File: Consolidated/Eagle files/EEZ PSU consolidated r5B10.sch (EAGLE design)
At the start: 542 parts, among them IC1 LTC3864EMSE#PBF, IC10 REF5025AIDG4, IC11 DAC8552IDGKTG4, IC12 ADG465SOT-23, IC13 TS5A9411DCKT, IC14 ADS1120IPWR, IC15 LP339D, IC16 LM25575MH/NOPB, IC17 TPD4E002DRLR, IC18 TPD2E001DZDR, IC19 ADUM3160BRWZ, IC2 MC79L05, IC20 TLC5925IDBQR, IC21 Si8641EC-B-IS1, IC22 SI8651EC-B-IS1, IC23 SI8651EC-B-IS1, IC24 LD1117ADT33TR, IC25 Si8641EC-B-IS1, IC26 PCA21125T/Q900/1,1, IC27 AT25256B-SSHL-B, IC28 W5500, IC29 BC857BS, IC3 MC78L05, IC30 TLC555, IC31 SN74LVC2G08DCTR, IC32 TPS3705-33D, IC33 SN74LV1T34DBVR, IC34 SN74LVC2G02DCTR, IC4 LM5574MTX/NOPB, IC5 LP2951SO8, IC6 TL072D, IC7 TL072D, IC8 OP27GSZ, IC9 MCP23S08-E/SO, J1 BS-244DSM-R, J2 BS-244DSM-G, J3 BS-244DSM-B, J4 BS-244DSM-R, J5 BS-244DSM-B, Q1 IRFR5305, Q10 MMBT5401, Q11 MMBT5401, Q12 MMBT5551, Q13 MMBT5551, Q14 BSS84P, Q15 2N7002, Q16 MMBT5551, Q17 MMBT5401, Q18 MMBT5551, Q19 MMBT5551, Q2 MMBT5401, Q20 BTA26-600, Q21 BTA26-600, Q22 IRLL014N, Q23 IRLML2246TRPBF, Q24 IRLML2246TRPBF, Q25 IRLML2246TRPBF, Q26 IRLML2246TRPBF, Q27 2N7002, Q28 IRLML2246TRPBF, Q29 2N7002, Q3 2N7002, Q30 2N7002, Q4 IRFP250N, Q5 BC857C, Q6 BC846C, Q7 BCP56-16.115, Q8 IRFR5410, Q9 BCP56-16.115, SW1 A101SYCQ04, SW2 1301.9316, X1 39303035, X10 826629-5, X11 2411-01, X12 MC000006, X13 TSW-113-07-F-D, X14 MC000005, X15 TSW-113-07-F-D, X16 09185067324, X17 22-23-2021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

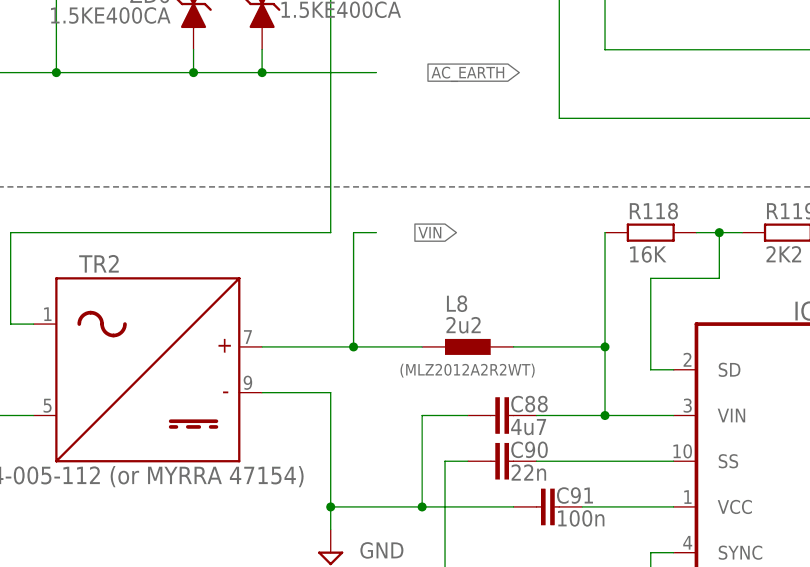
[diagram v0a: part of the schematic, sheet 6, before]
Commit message: r5B10 BOM, top silkscreen minor correction
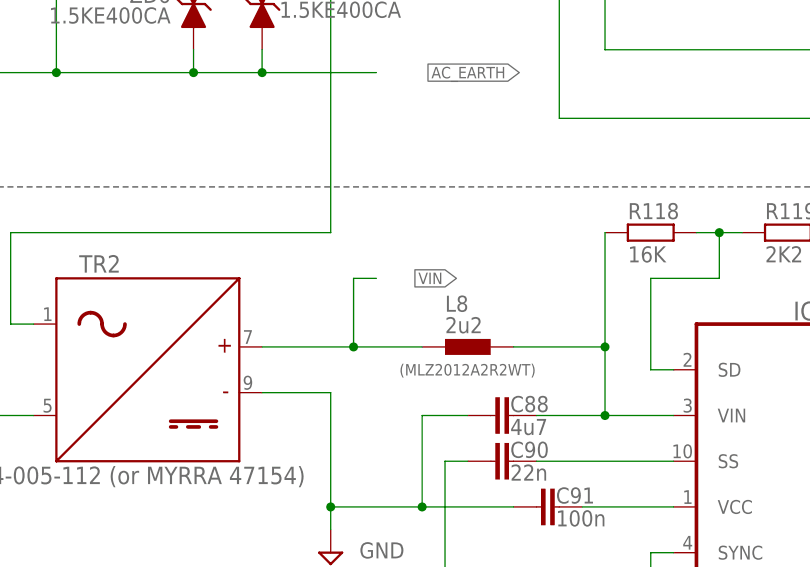
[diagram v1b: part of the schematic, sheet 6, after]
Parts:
- renumbered R136A1 to R140A
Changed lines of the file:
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@@
 <part name="R136A" library="rcl" deviceset="R-EU_" device="R0805" value="1R"/>
 <part name="C109A" library="rcl" deviceset="C-EU" device="C0805" value="1u"/>
-<part name="R136A1" library="rcl" deviceset="R-EU_" device="R0805" value="1R"/>
+<part name="R140A" library="rcl" deviceset="R-EU_" device="R0805" value="1R"/>
 <part name="C111" library="Panasonic-EEEFK_EEEFP" deviceset="EEE-" device="-CASE-E" technology="FK1J220P" value="EEEFK1J220P"/>
 <part name="C106" library="Panasonic-EEEFK_EEEFP" deviceset="EEE-" device="-CASE-E" technology="FK1J220P" value="EEEFK1J220P"/>
@@
 <pinref part="L8" gate="G$1" pin="1"/>
 <wire x1="83.82" y1="91.44" x2="76.2" y2="91.44" width="0.1524" layer="91"/>
-<wire x1="76.2" y1="91.44" x2="76.2" y2="104.14" width="0.1524" layer="91"/>
-<wire x1="76.2" y1="104.14" x2="78.74" y2="104.14" width="0.1524" layer="91"/>
-<label x="87.63" y="104.14" size="1.27" layer="102" rot="R180" xref="yes"/>
+<wire x1="76.2" y1="91.44" x2="76.2" y2="99.06" width="0.1524" layer="91"/>
+<wire x1="76.2" y1="99.06" x2="78.74" y2="99.06" width="0.1524" layer="91"/>
+<label x="87.63" y="99.06" size="1.27" layer="102" rot="R180" xref="yes"/>
 <pinref part="TR2" gate="TR1" pin="+"/>
 <wire x1="66.04" y1="91.44" x2="76.2" y2="91.44" width="0.1524" layer="91"/>
@@
 <attribute name="VALUE" x="75.819" y="38.354" size="1.778" layer="96" rot="MR180"/>
 </instance>
-<instance part="R136A1" gate="G$1" x="73.66" y="27.94" smashed="yes" rot="MR90">
+<instance part="R140A" gate="G$1" x="73.66" y="27.94" smashed="yes" rot="MR90">
 <attribute name="NAME" x="74.93" y="29.6164" size="1.778" layer="95" rot="MR180"/>
 <attribute name="VALUE" x="74.93" y="27.432" size="1.778" layer="96" rot="MR180"/>
@@
 <pinref part="K_SER" gate="-1" pin="S"/>
 <pinref part="C112" gate="G$1" pin="2"/>
-<pinref part="R136A1" gate="G$1" pin="1"/>
+<pinref part="R140A" gate="G$1" pin="1"/>
 <wire x1="73.66" y1="22.86" x2="73.66" y2="15.24" width="0.1524" layer="91"/>
 <wire x1="73.66" y1="15.24" x2="81.28" y2="15.24" width="0.1524" layer="91"/>
@@
 <segment>
 <pinref part="C109A" gate="G$1" pin="2"/>
-<pinref part="R136A1" gate="G$1" pin="2"/>
+<pinref part="R140A" gate="G$1" pin="2"/>
 <wire x1="73.66" y1="33.02" x2="73.66" y2="35.56" width="0.1524" layer="91"/>
 </segment>
